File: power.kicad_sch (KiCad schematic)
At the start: 42 parts

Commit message: Updated MCU
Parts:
- added C15, C19: 1uF, SOT-23-5_MC_MCH, symbol Device:C
- added U5: MIC5504-3.3YM5-TR, SOT-23-5_MC_MCH, symbol 2026-09-18_23-52-43:MIC5504-3.3YM5-TR
- renumbered B5 to B1, B1 to B2, B2 to B3, B3 to B4, B4 to B5, C23 to C14, C12 to C16, C24 to C17, C27 to C18, C25 to C20, C28 to C21, C35 to C22, C39 to C23, C43 to C24, C29 to C25, C36 to C26, C40 to C27, C30 to C28, C44 to C29, C31 to C30, C45 to C31, C37 to C33, C41 to C34, C33 to C35, C46 to C36, C34 to C37, C42 to C39, R18 to R14, R11 to R15, R13 to R16, R19 to R17, R16 to R18, R12 to R19, R17 to R20, R20 to R21, R21 to R22
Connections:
- net +5.2V: now also C15.1, U5.1 (VIN), U5.3 (EN)
- net GND: now also C15.2, C19.2, U5.2 (GND)
- new net +3.3V: C19.1, U5.5 (VOUT)
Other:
- note added: "3.3V LDO"

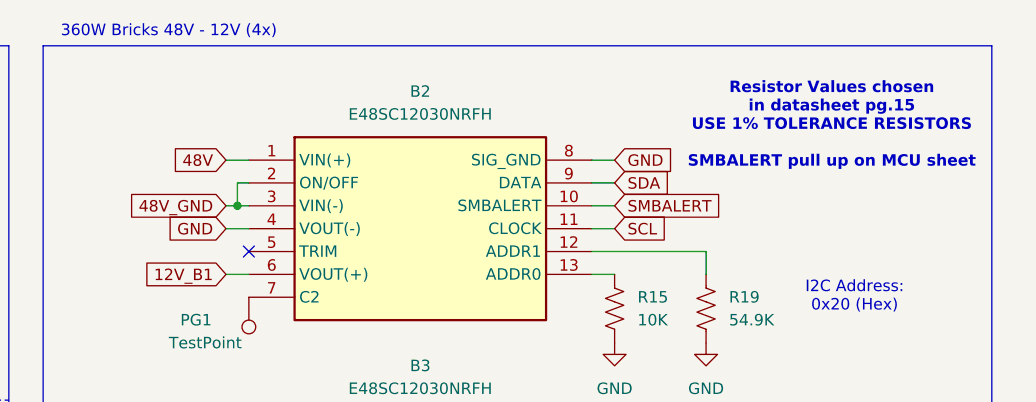
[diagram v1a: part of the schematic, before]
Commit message: Add INA237 for 12V for each brick
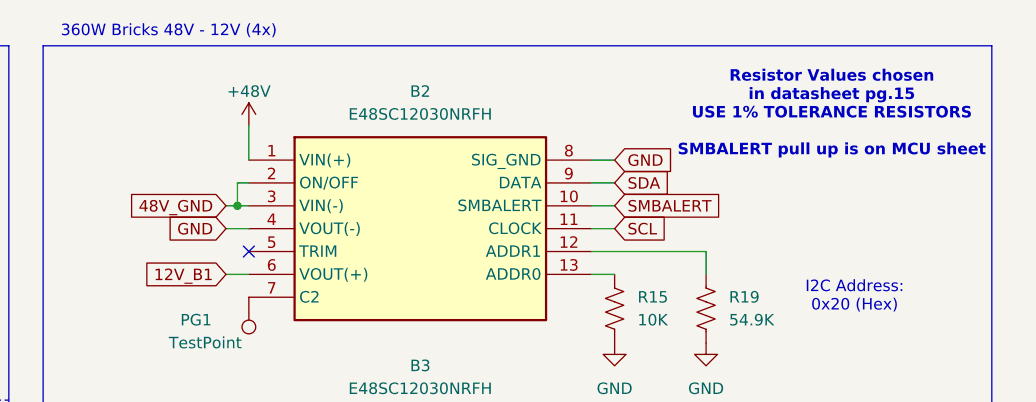
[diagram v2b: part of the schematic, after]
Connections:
- net +48V: now also B2.1 (VIN(+))
- net 48V: no longer B2.1 (VIN(+))
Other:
- note added: "Resistor Values chosen in datasheet pg.15 USE 1% TOLERANCE RESISTORS SMBALERT pull up is on MCU sheet"
- note removed: "Resistor Values chosen in datasheet pg.15 USE 1% TOLERANCE RESISTORS SMBALERT pull up on MCU sheet"
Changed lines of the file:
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@@
 		)
 	)
-	(text "Resistor Values chosen \nin datasheet pg.15\nUSE 1% TOLERANCE RESISTORS\n\nSMBALERT pull up on MCU sheet"
+	(text "Resistor Values chosen \nin datasheet pg.15\nUSE 1% TOLERANCE RESISTORS\n\nSMBALERT pull up is on MCU sheet"
 		(exclude_from_sim no)
-		(at 266.7 38.1 0)
+		(at 266.7 36.83 0)
 		(effects
 			(font
@@
 	(wire
 		(pts
+			(xy 201.93 38.1) (xy 201.93 41.91)
+		)
+		(stroke
+			(width 0)
+			(type default)
+		)
+	)
+	(wire
+		(pts
 			(xy 240.03 80.01) (xy 242.57 80.01)
 		)
@@
 	(wire
 		(pts
-			(xy 199.39 41.91) (xy 201.93 41.91)
-		)
-		(stroke
-			(width 0)
-			(type default)
-		)
-	)
-	(wire
-		(pts
 			(xy 240.03 85.09) (xy 242.57 85.09)
 		)
@@
 		)
 	)
-	(global_label "48V"
-		(shape input)
-		(at 199.39 41.91 180)
-		(fields_autoplaced yes)
-		(effects
-			(font
-				(size 1.27 1.27)
-			)
-			(justify right)
-		)
-		(property "Intersheetrefs" "${INTERSHEET_REFS}"
-			(at 192.8972 41.91 0)
-			(hide yes)
-			(show_name no)
-			(do_not_autoplace no)
-			(effects
-				(font
-					(size 1.27 1.27)
-				)
-				(justify right)
-			)
-		)
-	)
 	(global_label "48V_GND"
 		(shape input)
@@
 					(unit 1)
 				)
+			)
+		)
+	)
+	(symbol
+		(lib_id "power:+48V")
+		(at 201.93 38.1 0)
+		(unit 1)
+		(body_style 1)
+		(exclude_from_sim no)
+		(in_bom yes)
+		(on_board yes)
+		(in_pos_files yes)
+		(dnp no)
+		(property "Reference" "#PWR0106"
+			(at 201.93 41.91 0)
+			(hide yes)
+			(show_name no)
+			(do_not_autoplace no)
+			(effects
+				(font
+					(size 1.27 1.27)
+				)
+			)
+		)
+		(property "Value" "+48V"
+			(at 201.93 34.29 0)
+			(show_name no)
+			(do_not_autoplace no)
+			(effects
+				(font
+					(size 1.27 1.27)
+				)
+			)
+		)
+		(property "Footprint" ""
+			(at 201.93 38.1 0)
+			(hide yes)
+			(show_name no)
+			(do_not_autoplace no)
+			(effects
+				(font
+					(size 1.27 1.27)
+				)
+			)
+		)
+		(property "Datasheet" ""
+			(at 201.93 38.1 0)
+			(hide yes)
+			(show_name no)
+			(do_not_autoplace no)
+			(effects
+				(font
+					(size 1.27 1.27)
+				)
+			)
+		)
+		(property "Description" "Power symbol creates a global label with name \"+48V\""
+			(at 201.93 38.1 0)
+			(hide yes)
+			(show_name no)
+			(do_not_autoplace no)
+			(effects
+				(font
+					(size 1.27 1.27)
+				)
+			)
+		)
+		(pin "1"
+		)
+		(instances
+			(project "X19-Power-Slab-Board"
+				(path "/00000000-0000-0000-0000-000060e6118b/40111513-3970-440d-907d-e16164745ccd"
+					(reference "#PWR0106")
+					(unit 1)
+				)

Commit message: work mf
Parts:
- R14: value 404K -> 787K
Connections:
- removed net SMBALERT: B2.10 (SMBALERT), B3.10 (SMBALERT), B4.10 (SMBALERT), B5.10 (SMBALERT)
- new net SMBALERT_B2: B2.10 (SMBALERT)
- new net SMBALERT_B3: B3.10 (SMBALERT)
- new net SMBALERT_B4: B4.10 (SMBALERT)
- new net SMBALERT_B5: B5.10 (SMBALERT)
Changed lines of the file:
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@@
 		)
 	)
-	(global_label "SMBALERT"
+	(global_label "SMBALERT_B3"
 		(shape input)
 		(at 242.57 77.47 0)
@@
 		)
 		(property "Intersheetrefs" "${INTERSHEET_REFS}"
-			(at 254.9894 77.47 0)
+			(at 258.4365 77.47 0)
 			(hide yes)
 			(show_name no)
@@
 		)
 	)
-	(global_label "SMBALERT"
+	(global_label "SMBALERT_B5"
 		(shape input)
 		(at 242.57 143.51 0)
@@
 		)
 		(property "Intersheetrefs" "${INTERSHEET_REFS}"
-			(at 254.9894 143.51 0)
+			(at 258.4365 143.51 0)
 			(hide yes)
 			(show_name no)
@@
 		)
 	)
-	(global_label "SMBALERT"
+	(global_label "SMBALERT_B4"
 		(shape input)
 		(at 242.57 110.49 0)
@@
 		)
 		(property "Intersheetrefs" "${INTERSHEET_REFS}"
-			(at 254.9894 110.49 0)
+			(at 258.4365 110.49 0)
 			(hide yes)
 			(show_name no)
@@
 		)
 	)
-	(global_label "SMBALERT"
+	(global_label "SMBALERT_B2"
 		(shape input)
 		(at 242.57 46.99 0)
@@
 		)
 		(property "Intersheetrefs" "${INTERSHEET_REFS}"
-			(at 254.9894 46.99 0)
+			(at 258.4365 46.99 0)
 			(hide yes)
 			(show_name no)
@@
 			)
 		)
-		(property "Value" "404K"
+		(property "Value" "787K"
 			(at 52.07 166.37 90)
 			(show_name no)

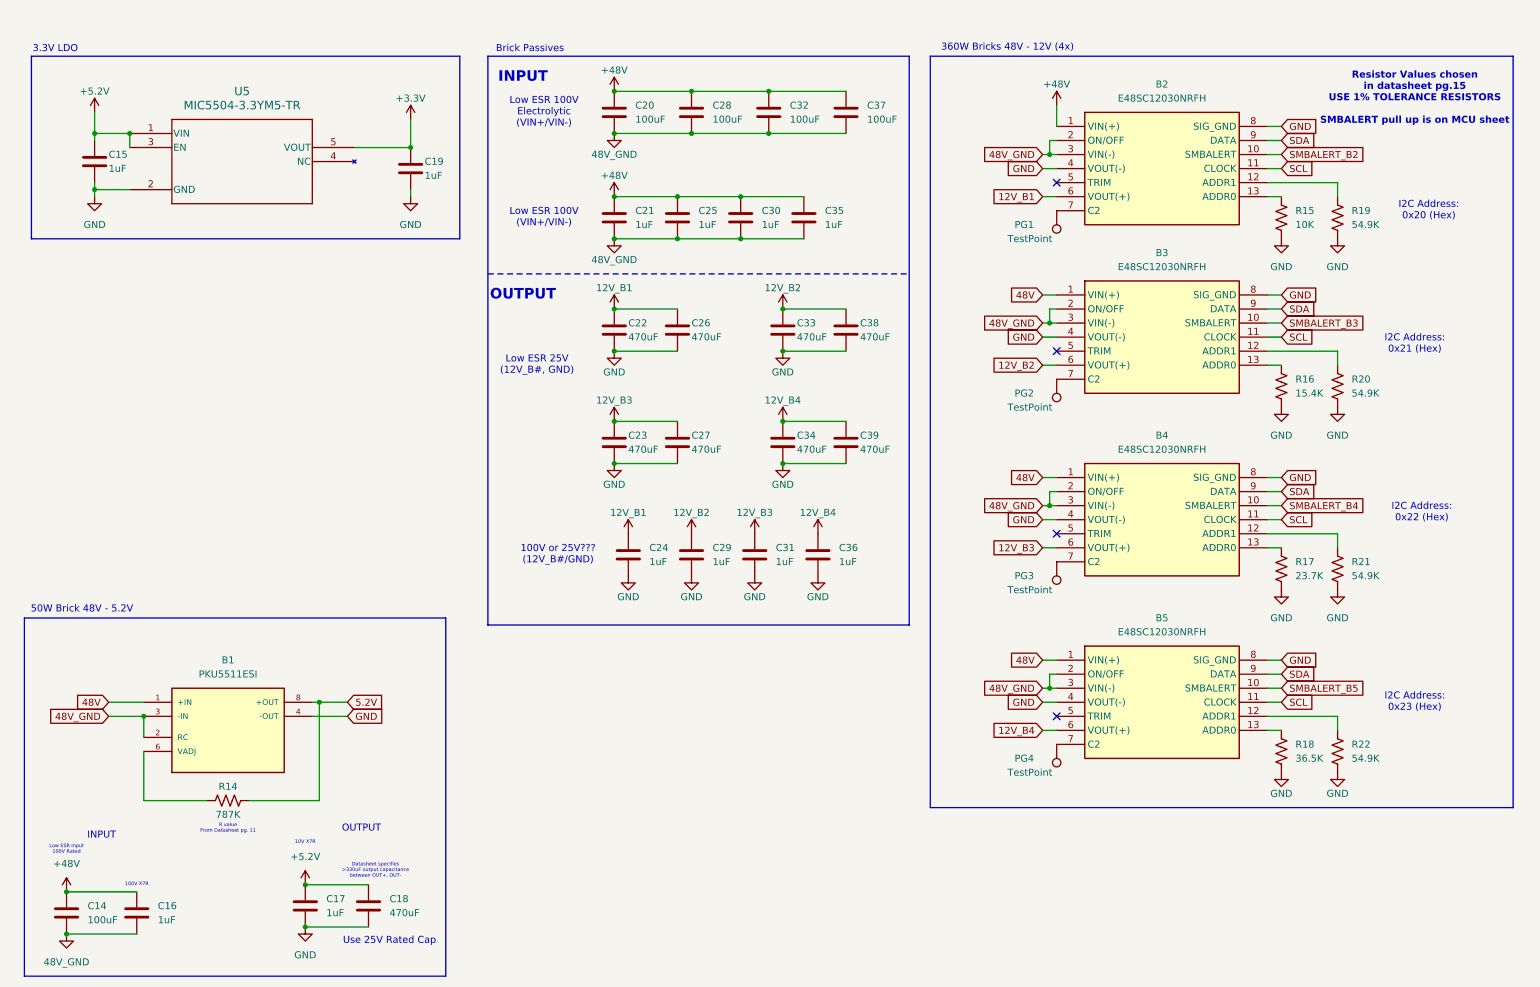
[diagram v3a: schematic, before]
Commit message: Added decouping caps
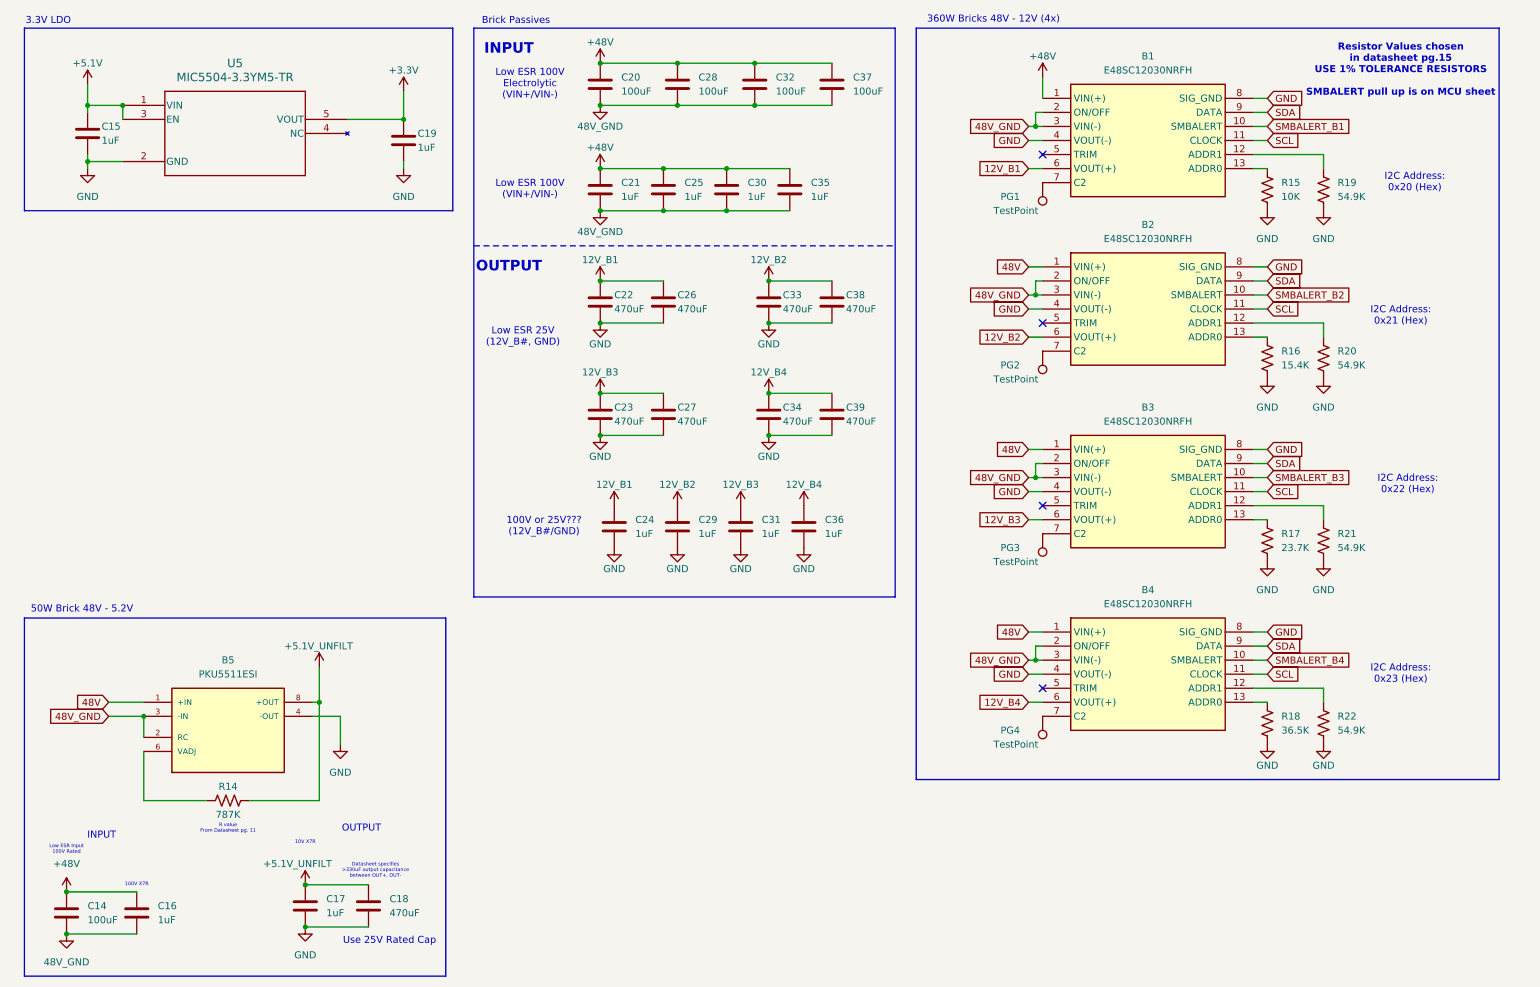
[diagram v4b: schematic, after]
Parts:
- renumbered B2 to B1, B3 to B2, B4 to B3, B5 to B4, B1 to B5
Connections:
- net SMBALERT_B5 is gone; now on net SMBALERT_B4: B4.10 (SMBALERT)
- net SMBALERT_B2: now also B2.10 (SMBALERT); no longer B1.10 (SMBALERT)
- net SMBALERT_B3: now also B3.10 (SMBALERT); no longer B2.10 (SMBALERT)
- net SMBALERT_B4: no longer B3.10 (SMBALERT)
- net +5.2V renamed +5.1V
- net +5.1V: no longer C17.1, C18.1
- net 5.2V renamed +5.1V_UNFILT
- net +5.1V_UNFILT: now also C17.1, C18.1
- new net SMBALERT_B1: B1.10 (SMBALERT)
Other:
- moved on the sheet: B1, B2, B3, B4, C15, C19, C20, C21, C22, C23, C24, C25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

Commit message: Reverse polarity and power flow TBD, improved capacitance and labelling for nets
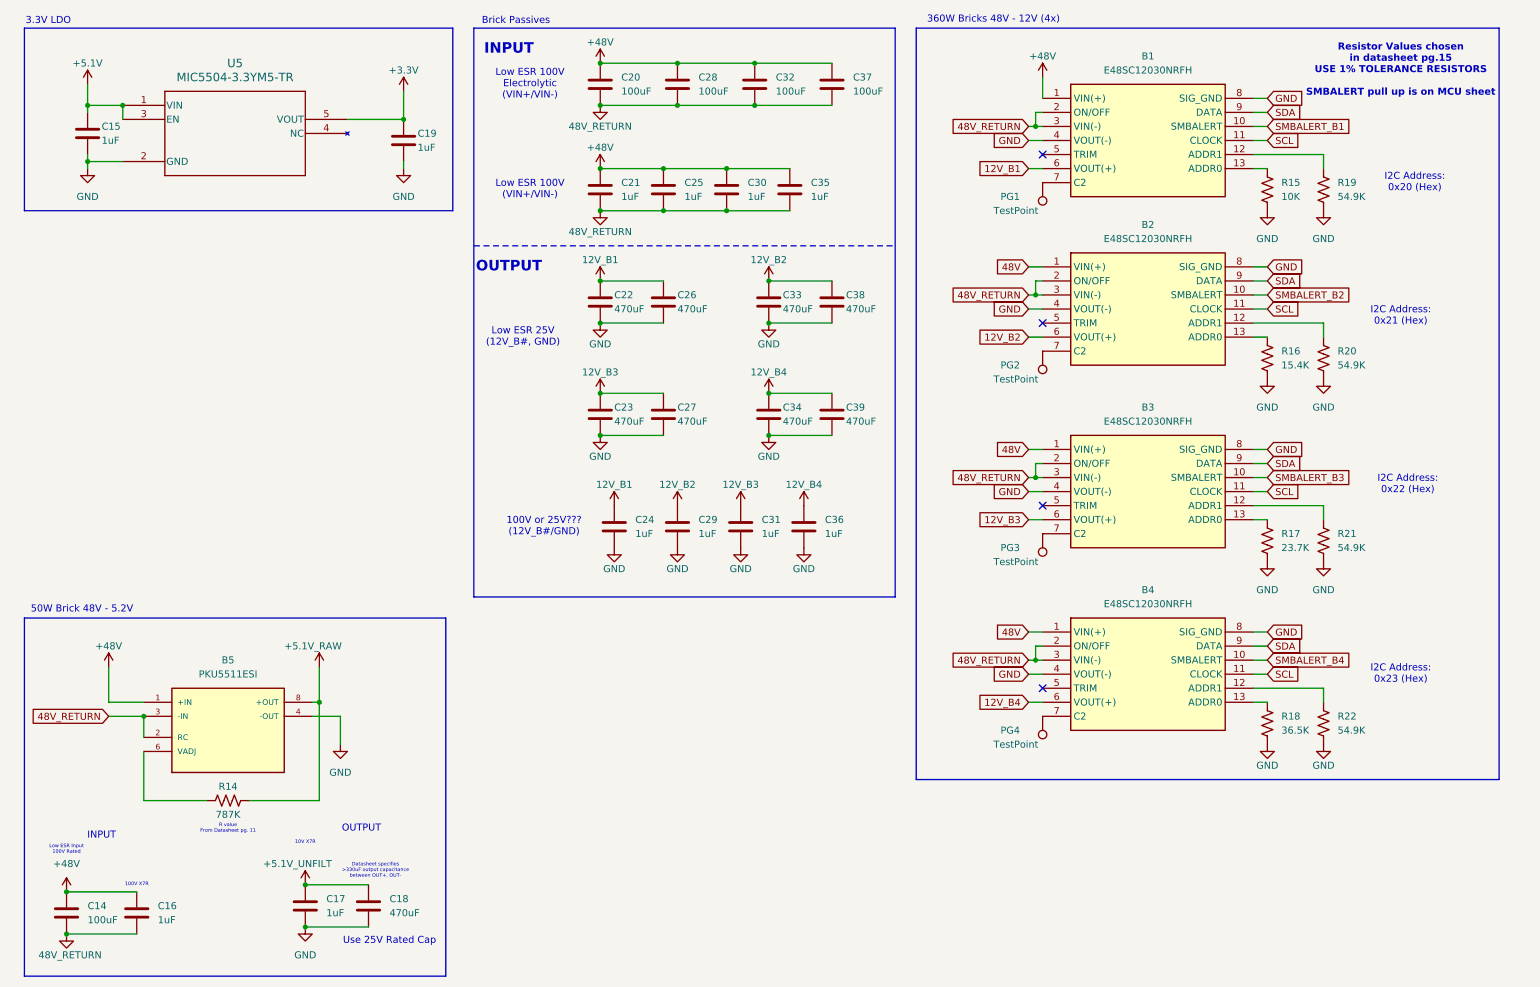
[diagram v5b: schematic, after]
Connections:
- net +48V: now also B5.1 (+IN)
- net +5.1V_UNFILT: no longer B5.8 (+OUT), R14.2
- net 48V: no longer B5.1 (+IN)
- net 48V_GND renamed 48V_RETURN
- new net +5.1V_RAW: B5.8 (+OUT), R14.2
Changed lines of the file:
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@@
 	(wire
 		(pts
+			(xy 30.48 139.7) (xy 30.48 146.05)
+		)
+		(stroke
+			(width 0)
+			(type default)
+		)
+	)
+	(wire
+		(pts
 			(xy 237.49 135.89) (xy 240.03 135.89)
 		)
@@
 		)
 	)
-	(global_label "48V_GND"
+	(global_label "48V_RETURN"
 		(shape input)
 		(at 196.85 72.39 180)
@@
 		)
 		(property "Intersheetrefs" "${INTERSHEET_REFS}"
-			(at 185.5191 72.39 0)
+			(at 182.072 72.39 0)
 			(hide yes)
 			(show_name no)
@@
 		)
 	)
-	(global_label "48V_GND"
+	(global_label "48V_RETURN"
 		(shape input)
 		(at 196.85 105.41 180)
@@
 		)
 		(property "Intersheetrefs" "${INTERSHEET_REFS}"
-			(at 185.5191 105.41 0)
+			(at 182.072 105.41 0)
 			(hide yes)
 			(show_name no)
@@
 		)
 	)
-	(global_label "48V_GND"
+	(global_label "48V_RETURN"
 		(shape input)
 		(at 30.48 148.59 180)
@@
 		)
 		(property "Intersheetrefs" "${INTERSHEET_REFS}"
-			(at 19.1491 148.59 0)
+			(at 15.702 148.59 0)
 			(hide yes)
 			(show_name no)
@@
 		)
 	)
-	(global_label "48V_GND"
+	(global_label "48V_RETURN"
 		(shape input)
 		(at 196.85 41.91 180)
@@
 		)
 		(property "Intersheetrefs" "${INTERSHEET_REFS}"
-			(at 185.5191 41.91 0)
-			(hide yes)
-			(show_name no)
-			(do_not_autoplace no)
-			(effects
-				(font
-					(size 1.27 1.27)
-				)
-				(justify right)
-			)
-		)
-	)
-	(global_label "48V"
-		(shape input)
-		(at 30.48 146.05 180)
-		(fields_autoplaced yes)
-		(effects
-			(font
-				(size 1.27 1.27)
-			)
-			(justify right)
-		)
-		(property "Intersheetrefs" "${INTERSHEET_REFS}"
-			(at 23.9872 146.05 0)
+			(at 182.072 41.91 0)
 			(hide yes)
 			(show_name no)
@@
 		)
 	)
-	(global_label "48V_GND"
+	(global_label "48V_RETURN"
 		(shape input)
 		(at 196.85 138.43 180)
@@
 		)
 		(property "Intersheetrefs" "${INTERSHEET_REFS}"
-			(at 185.5191 138.43 0)
+			(at 182.072 138.43 0)
 			(hide yes)
 			(show_name no)
@@
 			)
 		)
-		(property "Value" "+5.1V_UNFILT"
+		(property "Value" "+5.1V_RAW"
 			(at 62.23 135.89 0)
 			(show_name no)
@@
 			)
 		)
-		(property "Value" "48V_GND"
+		(property "Value" "48V_RETURN"
 			(at 119.38 60.96 0)
 			(show_name no)
@@
 	)
 	(symbol
+		(lib_id "power:+48V")
+		(at 30.48 139.7 0)
+		(unit 1)
+		(body_style 1)
+		(exclude_from_sim no)
+		(in_bom yes)
+		(on_board yes)
+		(in_pos_files yes)
+		(dnp no)
+		(property "Reference" "#PWR0127"
+			(at 30.48 143.51 0)
+			(hide yes)
+			(show_name no)
+			(do_not_autoplace no)
+			(effects
+				(font
+					(size 1.27 1.27)
+				)
+			)
+		)
+		(property "Value" "+48V"
+			(at 30.48 135.89 0)
+			(show_name no)
+			(do_not_autoplace no)
+			(effects
+				(font
+					(size 1.27 1.27)
+				)
+			)
+		)
+		(property "Footprint" ""
+			(at 30.48 139.7 0)
+			(hide yes)
+			(show_name no)
+			(do_not_autoplace no)
+			(effects
+				(font
+					(size 1.27 1.27)
+				)
+			)
+		)
+		(property "Datasheet" ""
+			(at 30.48 139.7 0)
+			(hide yes)
+			(show_name no)
+			(do_not_autoplace no)
+			(effects
+				(font
+					(size 1.27 1.27)
+				)
+			)
+		)
+		(property "Description" "Power symbol creates a global label with name \"+48V\""
+			(at 30.48 139.7 0)
+			(hide yes)
+			(show_name no)
+			(do_not_autoplace no)
+			(effects
+				(font
+					(size 1.27 1.27)
+				)
+			)
+		)
+		(pin "1"
+		)
+		(instances
+			(project "X19-Power-Slab-Board"
+				(path "/00000000-0000-0000-0000-000060e6118b/40111513-3970-440d-907d-e16164745ccd"
+					(reference "#PWR0127")
+					(unit 1)
+				)
+			)
+		)
+	)
+	(symbol
 		(lib_id "PKU5511ESI:PKU5511ESI")
 		(at 52.07 151.13 0)
@@
 		(in_pos_files yes)
 		(dnp no)
-		(fields_autoplaced yes)
 		(property "Reference" "#PWR059"
 			(at 22.86 194.31 0)
@@
 			)
 		)
-		(property "Value" "48V_GND"
-			(at 22.86 193.04 0)
+		(property "Value" "48V_RETURN"
+			(at 17.78 191.77 0)
 			(show_name no)
 			(do_not_autoplace no)
@@
 					(size 1.27 1.27)
 				)
+				(justify left)
 			)
 		)
@@
 			)
 		)
-		(property "Value" "48V_GND"
+		(property "Value" "48V_RETURN"
 			(at 119.38 41.91 0)
 			(show_name no)
